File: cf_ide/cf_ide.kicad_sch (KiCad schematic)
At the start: 17 parts, among them J1 PATA_44pin, J2 Compact_Flash_TrueIDE, U1 74AHC1G02, U2 LT1761-3.3

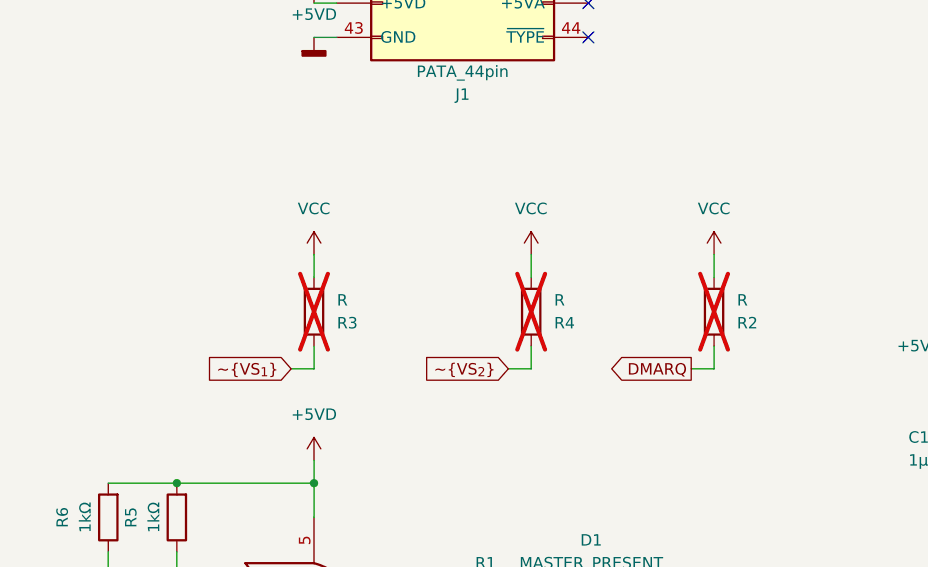
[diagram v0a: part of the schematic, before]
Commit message: Remove unneeded pull up/downs
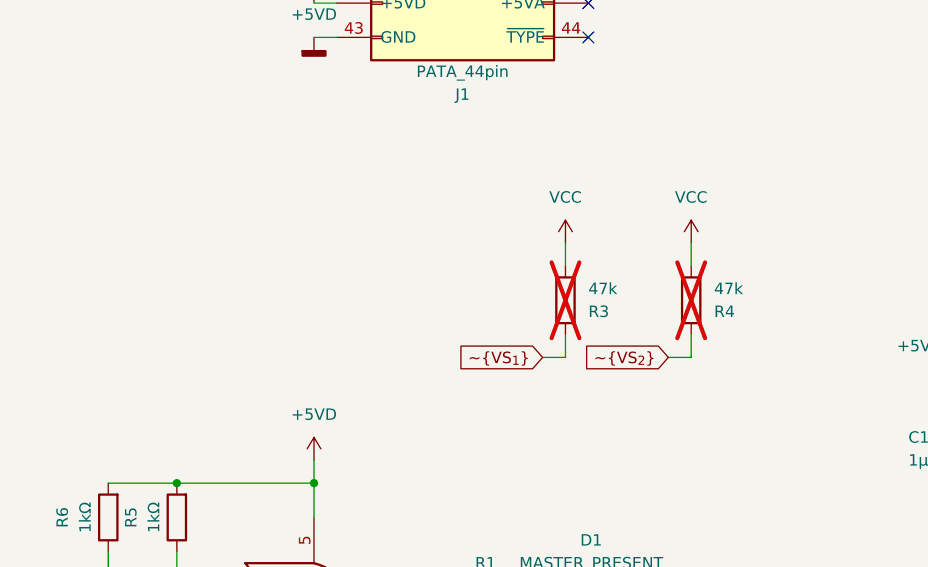
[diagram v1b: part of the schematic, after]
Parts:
- removed R2: R, Resistor_SMD:R_0603_1608Metric_Pad0.98x0.95mm_HandSolder, symbol Device:R
- R3, R4: value R -> 47k
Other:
- moved on the sheet: R3, R4

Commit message: Start PCB design
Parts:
- C1: footprint Capacitor_SMD:C_2220_5650Metric_Pad1.97x5.40mm_HandSolder -> Capacitor_SMD:C_0805_2012Metric_Pad1.18x1.45mm_HandSolder
- C2: value 0.1μF -> 0.01μF
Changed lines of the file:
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@@
 			)
 		)
-		(property "Footprint" "Capacitor_SMD:C_2220_5650Metric_Pad1.97x5.40mm_HandSolder"
+		(property "Footprint" "Capacitor_SMD:C_0805_2012Metric_Pad1.18x1.45mm_HandSolder"
 			(at 129.2352 158.75 0)
 			(effects
@@
 			)
 		)
-		(property "Value" "0.1μF"
+		(property "Value" "0.01μF"
 			(at 162.56 154.94 90)
 			(effects
